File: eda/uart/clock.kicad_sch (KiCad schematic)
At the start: 5 parts, among them U1 74HCT193, X1 1.8xx

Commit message: Port main board schematic to kicad
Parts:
- C2, C3, C4: footprint Capacitor_THT:C_Rect_L7.2mm_W2.5mm_P5.00mm_FKS2_FKP2_MKS2_MKP2 -> Capacitor_THT:C_Rect_L7.2mm_W3.5mm_P5.00mm_FKS2_FKP2_MKS2_MKP2

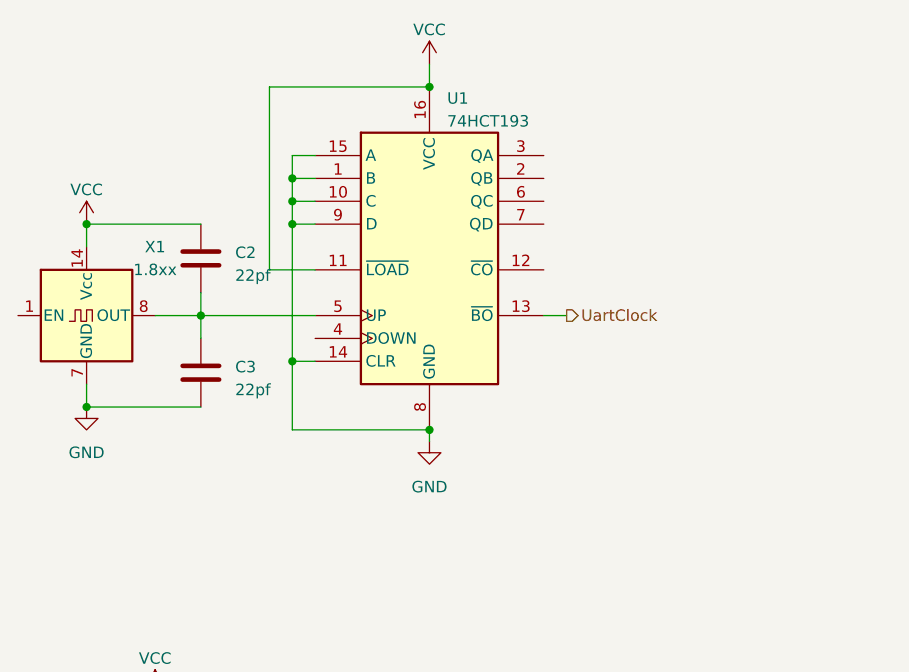
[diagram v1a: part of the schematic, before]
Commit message: Update UART transmit logic
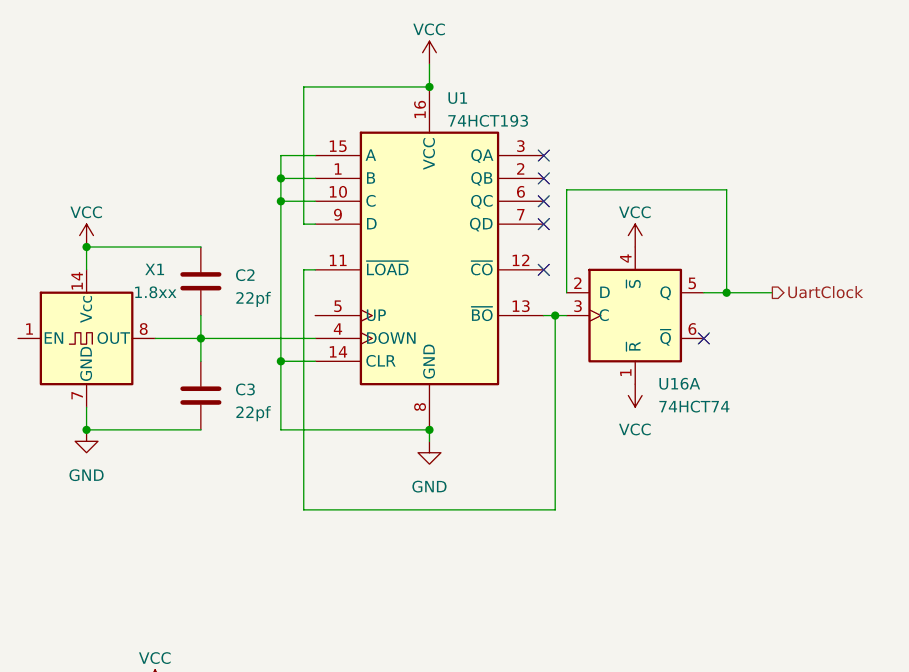
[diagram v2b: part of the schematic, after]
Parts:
- added U16: 74HCT74, Package_DIP:DIP-14_W10.16mm, symbol 74xx:74LS74
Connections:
- net GND: no longer U1.9 (D)
- net UartClock: now also U16.2 (D), U16.5 (Q); no longer U1.13 (~{BO})
- net VCC: now also U1.9 (D), U16.1 (~{R}), U16.4 (~{S}); no longer U1.11 (~{LOAD})
- net at C2.2, C3.1, X1.8 (OUT): now also U1.4 (DOWN); no longer U1.5 (UP)
- new net: U1.11 (~{LOAD}), U1.13 (~{BO}), U16.3 (C)
- no-connect marks 0 -> 6
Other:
- moved on the sheet: C2, C3, X1

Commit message: Sync
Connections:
- net UartClock: no longer U16.2 (D)
- net at U16.6 (~{Q}): now also U16.2 (D)
- no-connect marks 6 -> 5
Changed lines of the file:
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@@
   (junction (at 97.79 82.55) (diameter 0) (color 0 0 0 0)
-  )
-  (junction (at 130.81 67.31) (diameter 0) (color 0 0 0 0)
   )
   (junction (at 59.69 82.55) (diameter 0) (color 0 0 0 0)
@@
   (no_connect (at 110.49 54.61))
   (no_connect (at 110.49 59.69))
-  (no_connect (at 128.27 72.39))
+  (wire (pts (xy 130.81 72.39) (xy 128.27 72.39))
+    (stroke (width 0) (type default))
+  )
   (wire (pts (xy 72.39 69.85) (xy 72.39 72.39))
     (stroke (width 0) (type default))
@@
     (stroke (width 0) (type default))
   )
-  (wire (pts (xy 135.89 67.31) (xy 130.81 67.31))
-    (stroke (width 0) (type default))
-  )
-  (wire (pts (xy 130.81 67.31) (xy 128.27 67.31))
+  (wire (pts (xy 128.27 67.31) (xy 135.89 67.31))
     (stroke (width 0) (type default))
   )
@@
     (stroke (width 0) (type default))
   )
+  (wire (pts (xy 130.81 55.88) (xy 130.81 72.39))
+    (stroke (width 0) (type default))
+  )
   (wire (pts (xy 59.69 82.55) (xy 59.69 80.01))
     (stroke (width 0) (type default))
@@
   )
   (wire (pts (xy 111.76 91.44) (xy 111.76 69.85))
-    (stroke (width 0) (type default))
-  )
-  (wire (pts (xy 130.81 67.31) (xy 130.81 55.88))
     (stroke (width 0) (type default))
   )
@@
         )
         (path "/11545594-d6d6-4b37-a578-fa23933d5773/2c491a73-e75e-409f-b87e-2b908ecd3c3f"
-          (reference "U16") (unit 1)
-        )
-      )
+          (reference "U16") (unit 2)
+        )
+      )

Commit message: Normalize cap size
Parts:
- C2, C3, C4: footprint Capacitor_THT:C_Rect_L7.2mm_W3.5mm_P5.00mm_FKS2_FKP2_MKS2_MKP2 -> Capacitor_THT:C_Disc_D3.8mm_W2.6mm_P2.50mm
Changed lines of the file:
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@@
       (effects (font (size 1.27 1.27)) (justify left))
     )
-    (property "Footprint" "Capacitor_THT:C_Rect_L7.2mm_W3.5mm_P5.00mm_FKS2_FKP2_MKS2_MKP2" (at 73.3552 82.55 0)
+    (property "Footprint" "Capacitor_THT:C_Disc_D3.8mm_W2.6mm_P2.50mm" (at 73.3552 82.55 0)
       (effects (font (size 1.27 1.27)) hide)
     )
@@
       (effects (font (size 1.27 1.27)) (justify left))
     )
-    (property "Footprint" "Capacitor_THT:C_Rect_L7.2mm_W3.5mm_P5.00mm_FKS2_FKP2_MKS2_MKP2" (at 82.2452 120.65 0)
+    (property "Footprint" "Capacitor_THT:C_Disc_D3.8mm_W2.6mm_P2.50mm" (at 82.2452 120.65 0)
       (effects (font (size 1.27 1.27)) hide)
     )
@@
       (effects (font (size 1.27 1.27)) (justify left))
     )
-    (property "Footprint" "Capacitor_THT:C_Rect_L7.2mm_W3.5mm_P5.00mm_FKS2_FKP2_MKS2_MKP2" (at 73.3552 69.85 0)
+    (property "Footprint" "Capacitor_THT:C_Disc_D3.8mm_W2.6mm_P2.50mm" (at 73.3552 69.85 0)
       (effects (font (size 1.27 1.27)) hide)
     )

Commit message: Uart and loader work
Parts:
- renumbered C2 to C4, C3 to C5, C4 to C6, U1 to U3
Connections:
- net UartClock: now also U16.9 (Q); no longer U16.5 (Q)
- net VCC: now also U16.10 (~{S}), U16.13 (~{R}); no longer U16.1 (~{R}), U16.4 (~{S})
- net at U3.11 (~{LOAD}), U3.13 (~{BO}): now also U16.11 (C); no longer U16.3 (C)
- new net: U16.12 (D), U16.8 (~{Q})

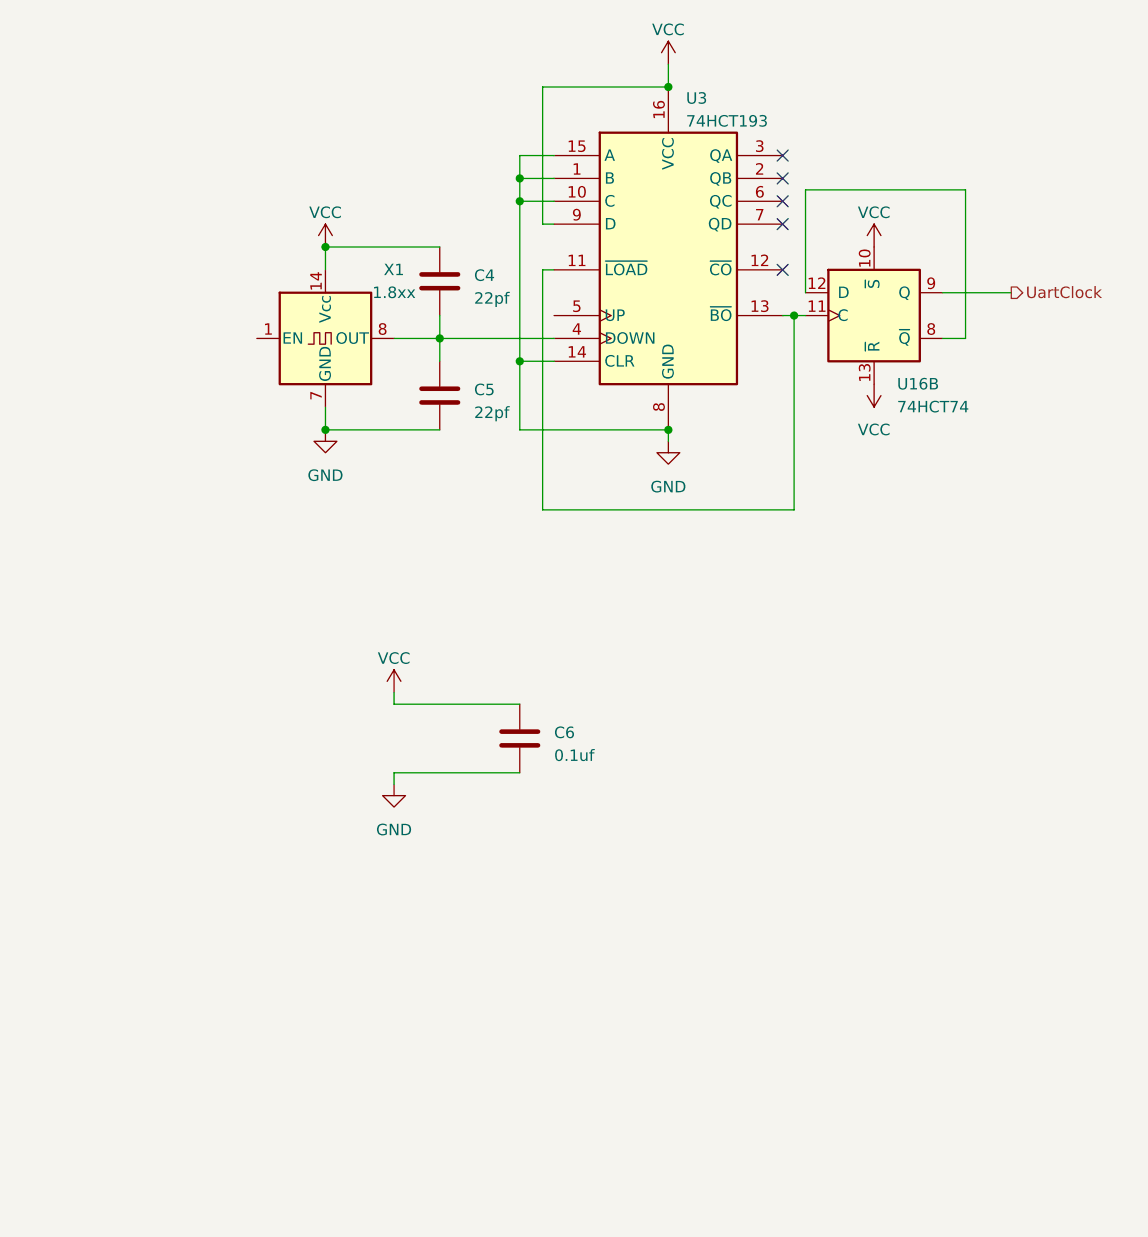
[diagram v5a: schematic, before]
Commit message: Uart board to v1.1...make bodges permanent :(
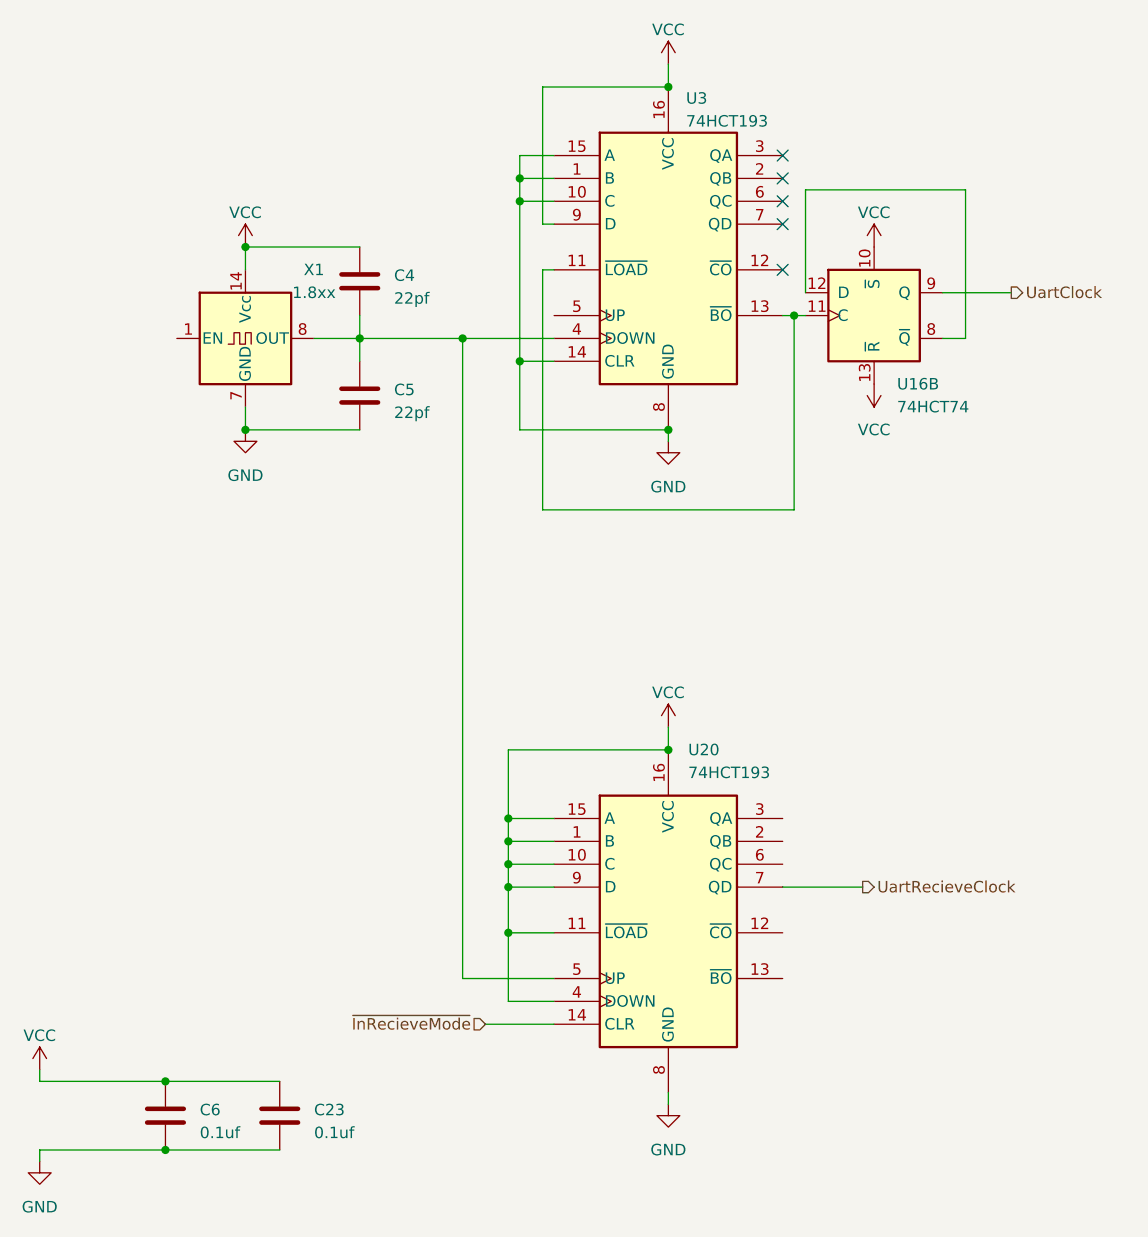
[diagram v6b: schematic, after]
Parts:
- added C23: 0.1uf, Capacitor_THT:C_Disc_D3.8mm_W2.6mm_P2.50mm, symbol Device:C
- added U20: 74HCT193, Package_DIP:DIP-16_W7.62mm, symbol 74xx:74LS193
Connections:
- net GND: now also C23.2, U20.8 (GND)
- net VCC: now also C23.1, U20.1 (B), U20.10 (C), U20.11 (~{LOAD}), U20.15 (A), U20.16 (VCC), U20.4 (DOWN), U20.9 (D)
- net at C4.2, C5.1, U3.4 (DOWN)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: now also U20.5 (UP)
- new net UartRecieveClock: U20.7 (QD)
- new net ~{InRecieveMode}: U20.14 (CLR)
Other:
- moved on the sheet: C4, C5, C6, X1
